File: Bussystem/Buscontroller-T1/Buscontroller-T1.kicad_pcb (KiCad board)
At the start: 2 copper layers, 1 part, among them J1 PCIE-098-02-X-D-TH

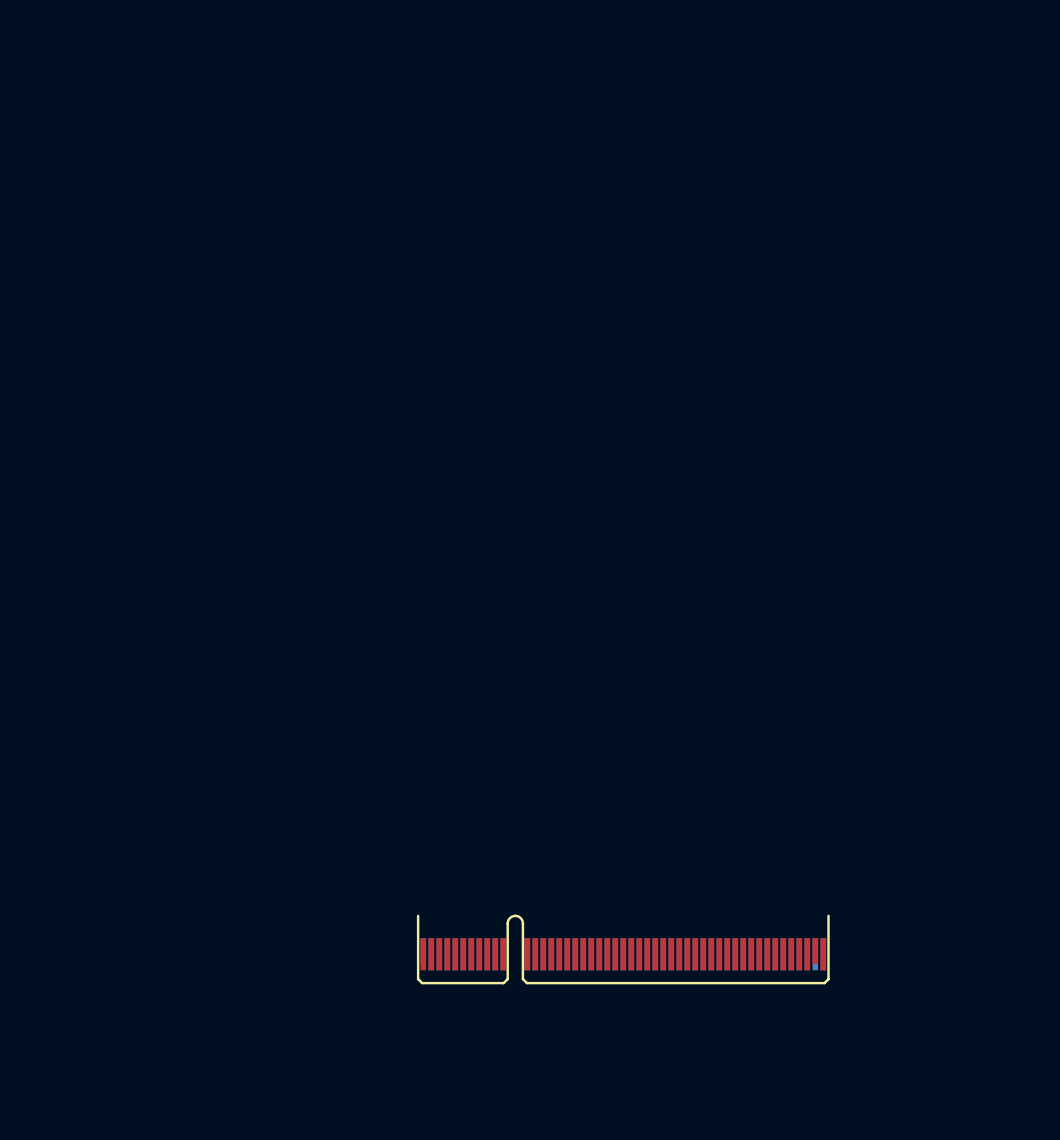
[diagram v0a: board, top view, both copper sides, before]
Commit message: some new parts in the Buscontroller T1
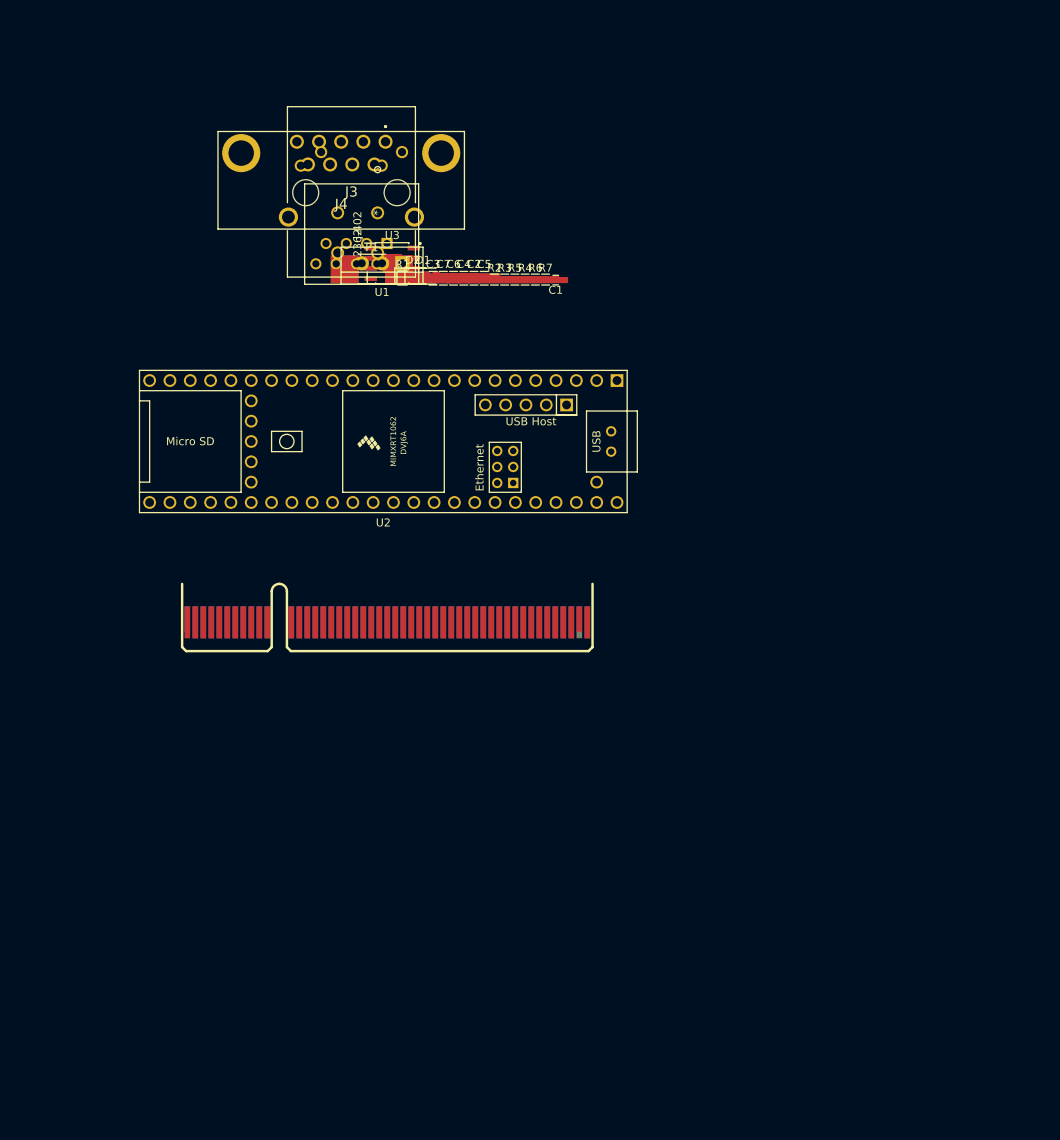
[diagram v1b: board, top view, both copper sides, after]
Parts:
- added C1: 100n, Capacitors_SMD:C_0603_HandSoldering, F.Cu at (125.5, 67.8)
- added C2: 4.7u, Capacitors_SMD:C_0805_HandSoldering, F.Cu at (115.3, 67.6)
- added C3: 100n, Capacitors_SMD:C_0805_HandSoldering, F.Cu at (110.2, 67.6)
- added C4: 100n, Capacitors_SMD:C_0805_HandSoldering, F.Cu at (114.1, 67.6)
- added C5: 100n, Capacitors_SMD:C_0805_HandSoldering, F.Cu at (116.6, 67.6)
- added C6: 100n, Capacitors_SMD:C_0805_HandSoldering, F.Cu at (112.8, 67.6)
- added C7: 4700p, Capacitors_SMD:C_0805_HandSoldering, F.Cu at (111.5, 67.6)
- added D1: 1N4148W, Diodes_SMD:D_SOD-123, F.Cu at (109.0, 67.3)
- added D2: 1N4148W, Diodes_SMD:D_SOD-123, F.Cu at (107.7, 67.3)
- added F1: mSMD050-60V, Resistors_SMD:R_1812_HandSoldering, F.Cu at (102.6, 66.5)
- added J2: 236-402, footprints:236-402, F.Cu at (103.3, 59.4)
- added J3: J1B1211CCD, SamacSys_Parts:J1B1211CCD, F.Cu at (100.0, 56.8)
- added J4: 2311765-1, SamacSys_Parts:23117651, F.Cu at (104.3, 50.5)
- added R1: 0R, Resistors_SMD:R_0805_HandSoldering, F.Cu at (106.4, 67.6)
- added R2: 60R, Resistors_SMD:R_0603_HandSoldering, F.Cu at (117.9, 67.8)
- added R3: 60R, Resistors_SMD:R_0603_HandSoldering, F.Cu at (119.2, 67.8)
- added R4: 1k, Resistors_SMD:R_0603_HandSoldering, F.Cu at (121.7, 67.8)
- added R5: 1k, Resistors_SMD:R_0603_HandSoldering, F.Cu at (120.4, 67.8)
- added R6: 120R, Resistors_SMD:R_0603_HandSoldering, F.Cu at (123.0, 67.8)
- added R7: 120R, Resistors_SMD:R_0603_HandSoldering, F.Cu at (124.3, 67.8)
- added U1: LM7805L-TF3-T, TO_SOT_Packages_THT:TO-220-3_Vertical, F.Cu at (106.4, 65.7)
- added U2: Teensy4.1, teensy:Teensy41, F.Cu at (104.0, 88.0)
- added U3: MCP2542FD, Housings_SOIC:SOIC-8-1EP_3.9x4.9mm_Pitch1.27mm, F.Cu at (105.1, 65.7)
- J1: value PCIE-098-02-X-D-TH -> PCIE-098-edge-conn
- moved J1 50.9 mm to (91.0, 110.0)
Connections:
- J1 pad A1: (no net) -> GND
- J1 pad A10: (no net) -> /CANL
- J1 pad A11: (no net) -> GND
- J1 pad A12: (no net) -> SPI_CS
- J1 pad A13: (no net) -> GND
- J1 pad A14: (no net) -> SPI_Sck
- J1 pad A15: (no net) -> GND
- J1 pad A16: (no net) -> SPI_MoSi
- J1 pad A17: (no net) -> GND
- J1 pad A18: (no net) -> SPI_MiSo
- J1 pad A19: (no net) -> GND
- J1 pad A2: (no net) -> GND
- J1 pad A20: (no net) -> /Do0
- J1 pad A21: (no net) -> /Do1
- J1 pad A22: (no net) -> /Do2
- J1 pad A23: (no net) -> /Do3
- J1 pad A24: (no net) -> /Do4
- J1 pad A25: (no net) -> /Do5
- J1 pad A26: (no net) -> /Do6
- J1 pad A27: (no net) -> /Do7
- J1 pad A28: (no net) -> /Di0
- J1 pad A29: (no net) -> /Di1
- J1 pad A3: (no net) -> /24V
- J1 pad A30: (no net) -> /Di2
- J1 pad A31: (no net) -> /Di3
- J1 pad A32: (no net) -> /Di4
- J1 pad A33: (no net) -> /Di5
- J1 pad A34: (no net) -> /Di6
- J1 pad A35: (no net) -> /Di7
- J1 pad A36: (no net) -> /Dclk
- J1 pad A37: (no net) -> /DWR
- J1 pad A38: (no net) -> Net-(J1-PadA38)
- J1 pad A39: (no net) -> Net-(J1-PadA39)
- J1 pad A4: (no net) -> /24V
- J1 pad A40: (no net) -> Net-(J1-PadA40)
- J1 pad A41: (no net) -> Net-(J1-PadA41)
- J1 pad A42: (no net) -> Net-(J1-PadA42)
- J1 pad A43: (no net) -> Net-(J1-PadA43)
- J1 pad A44: (no net) -> Net-(J1-PadA44)
- J1 pad A45: (no net) -> Net-(J1-PadA45)
- J1 pad A46: (no net) -> Net-(J1-PadA46)
- J1 pad A47: (no net) -> Net-(J1-PadA47)
- J1 pad A48: (no net) -> Net-(J1-PadA48)
- J1 pad A49: (no net) -> Net-(J1-PadA49)
- J1 pad A5: (no net) -> /24V
- J1 pad A6: (no net) -> Scl_I2C
- J1 pad A7: (no net) -> Sda_I2C
- J1 pad A8: (no net) -> /5V
- J1 pad A9: (no net) -> /CANH
- J1 pad B1: (no net) -> GND
- J1 pad B10: (no net) -> /CANL
- J1 pad B11: (no net) -> GND
- J1 pad B12: (no net) -> SPI_CS
- J1 pad B13: (no net) -> GND
- J1 pad B14: (no net) -> SPI_Sck
- J1 pad B15: (no net) -> GND
- J1 pad B16: (no net) -> SPI_MoSi
- J1 pad B17: (no net) -> GND
- J1 pad B18: (no net) -> SPI_MiSo
- J1 pad B19: (no net) -> GND
- J1 pad B2: (no net) -> GND
- J1 pad B20: (no net) -> /Do0
- J1 pad B21: (no net) -> /Do1
- J1 pad B22: (no net) -> /Do2
- J1 pad B23: (no net) -> /Do3
- J1 pad B24: (no net) -> /Do4
- J1 pad B25: (no net) -> /Do5
- J1 pad B26: (no net) -> /Do6
- J1 pad B27: (no net) -> /Do7
- J1 pad B28: (no net) -> /Di0
- J1 pad B29: (no net) -> /Di1
- J1 pad B3: (no net) -> /24V
- J1 pad B30: (no net) -> /Di2
- J1 pad B31: (no net) -> /Di3
- J1 pad B32: (no net) -> /Di4
- J1 pad B33: (no net) -> /Di5
- J1 pad B34: (no net) -> /Di6
- J1 pad B35: (no net) -> /Di7
- J1 pad B36: (no net) -> /Dclk
- J1 pad B37: (no net) -> /DWR
- J1 pad B38: (no net) -> Net-(J1-PadA38)
- J1 pad B39: (no net) -> Net-(J1-PadA39)
- J1 pad B4: (no net) -> /24V
- J1 pad B40: (no net) -> Net-(J1-PadA40)
- J1 pad B41: (no net) -> Net-(J1-PadA41)
- J1 pad B42: (no net) -> Net-(J1-PadA42)
- J1 pad B43: (no net) -> Net-(J1-PadA43)
- J1 pad B44: (no net) -> Net-(J1-PadA44)
- J1 pad B45: (no net) -> Net-(J1-PadA45)
- J1 pad B46: (no net) -> Net-(J1-PadA46)
- J1 pad B47: (no net) -> Net-(J1-PadA47)
- J1 pad B48: (no net) -> Net-(J1-PadA48)
- J1 pad B49: (no net) -> Net-(J1-PadA49)
- J1 pad B5: (no net) -> /24V
- J1 pad B6: (no net) -> Scl_I2C
- J1 pad B7: (no net) -> Sda_I2C
- J1 pad B8: (no net) -> /5V
- J1 pad B9: (no net) -> /CANH

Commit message: erstes import zum Layouten von Buscontroller
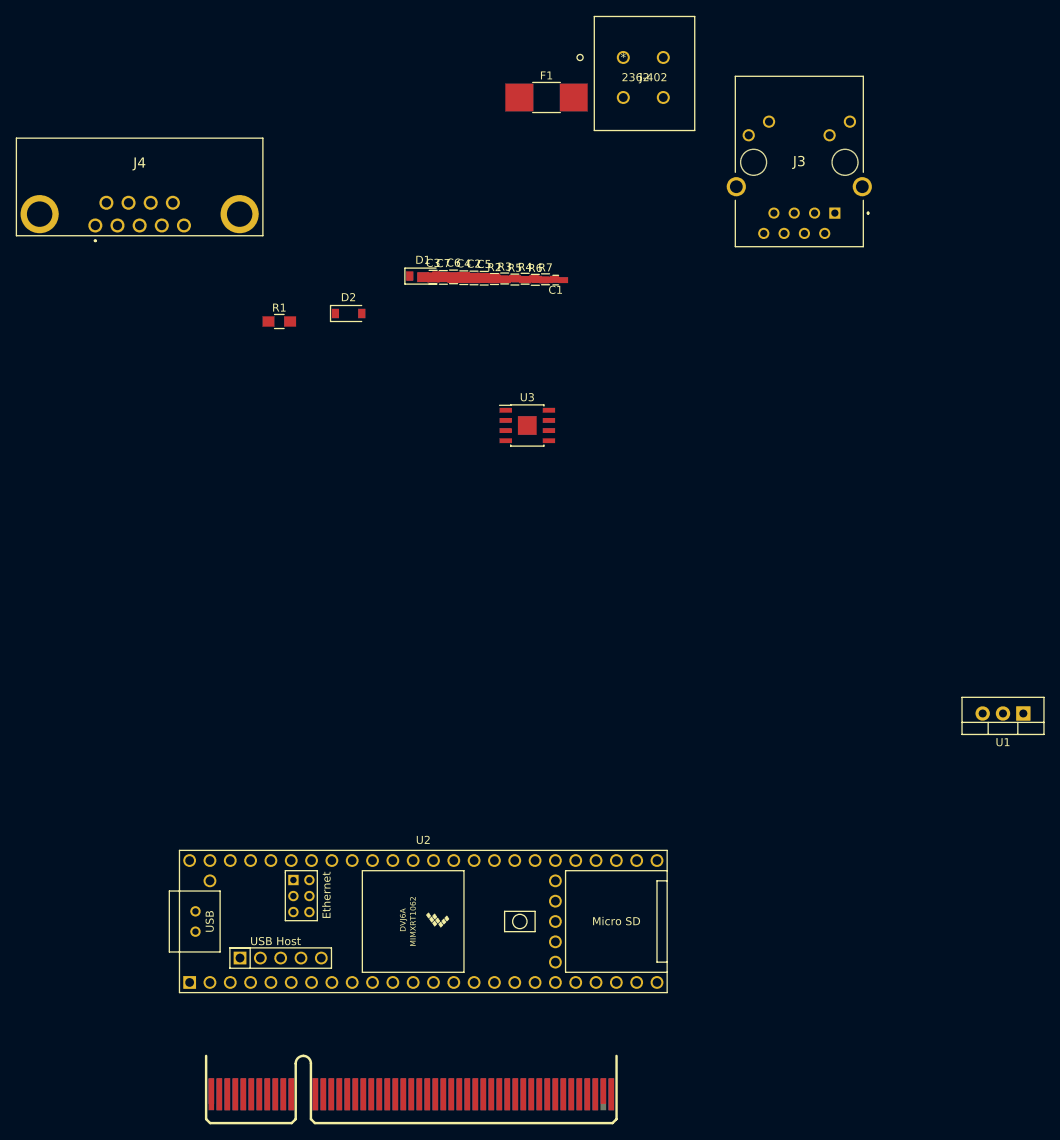
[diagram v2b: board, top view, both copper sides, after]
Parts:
- moved U1 95.9 mm to (184.0, 122.0)
- moved U2 60.2 mm to (109.0, 148.0), turned to 0 degrees
- moved J1 59.1 mm to (94.0, 169.0)
- moved J3 56.1 mm to (156.0, 53.0)
- moved J4 37.8 mm to (68.0, 61.0), turned to 180 degrees
- moved J2 36.3 mm to (134.0, 40.0), turned to 0 degrees
- moved F1 30.6 mm to (124.4, 45.0)
- moved U3 26.4 mm to (122.0, 86.0)
- moved R1 16.3 mm to (91.0, 73.0)
- moved D2 9.29 mm to (99.7, 72.0)
- moved C6 0.17 mm to (112.8, 67.4)
- moved R3 0.14 mm to (119.2, 67.6)
- moved C3 0.13 mm to (110.2, 67.5)
- moved R4 0.10 mm to (121.7, 67.7)
- moved C7 0.10 mm to (111.5, 67.5)
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
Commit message: buscontroller T1 fertig
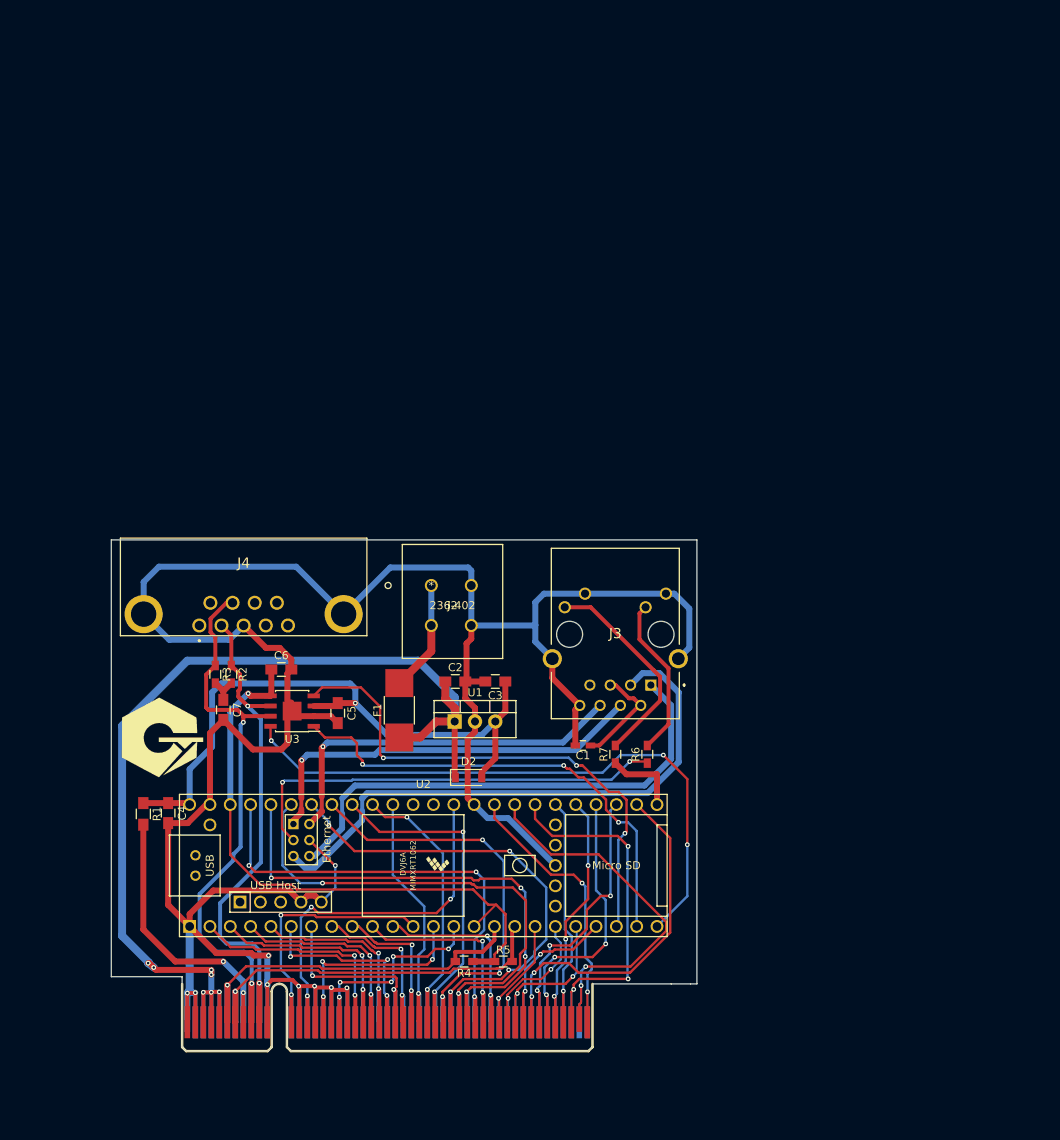
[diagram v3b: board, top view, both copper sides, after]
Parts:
- removed D1: 1N4148W, Diodes_SMD:D_SOD-123
- added G***: Gyurmas Electronix, Gyurmas:GyLogo2_1, F.Cu at (76.4, 125.0)
- J3: footprint SamacSys_Parts:J1B1211CCD -> J1B1211CCD
- J4: footprint SamacSys_Parts:23117651 -> 23117651
- moved R4 85.7 mm to (114.1, 153.0), turned to 180 degrees
- moved R5 85.3 mm to (119.0, 153.0)
- moved F1 78.8 mm to (106.0, 121.6), turned to 90 degrees
- moved C4 76.5 mm to (77.1, 134.4), turned to 270 degrees
- moved U1 71.1 mm to (112.9, 123.0), turned to 0 degrees
- moved J2 70.2 mm to (110.0, 106.0)
- moved R1 63.9 mm to (74.0, 134.6), turned to 270 degrees
- moved J3 63.3 mm to (133.0, 112.0)
- moved R3 61.3 mm to (83.0, 117.1), turned to 270 degrees
- moved R6 60.9 mm to (137.0, 127.1), turned to 90 degrees
- moved C7 60.7 mm to (84.0, 121.5), turned to 270 degrees
- moved R7 60.0 mm to (133.0, 127.1), turned to 90 degrees
- moved D2 59.9 mm to (114.7, 130.0)
- moved R2 59.4 mm to (85.0, 117.1), turned to 270 degrees
- moved C1 58.3 mm to (128.9, 126.0)
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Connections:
- net Net-(U2-Pad22) renamed /CANRX3
- net Net-(U2-Pad23) renamed /CANTX3
- net Net-(U2-Pad24) renamed /CANStby
- C4 pad 1: Net-(C4-Pad1) -> Net-(C3-Pad1)
- C5 pad 1: Net-(C4-Pad1) -> Net-(C3-Pad1)
- J1 pad A38: Net-(J1-PadA38) -> /D0
- J1 pad A39: Net-(J1-PadA39) -> /D1
- J1 pad A40: Net-(J1-PadA40) -> /D2
- J1 pad A41: Net-(J1-PadA41) -> /D3
- J1 pad A42: Net-(J1-PadA42) -> /D4
- J1 pad A43: Net-(J1-PadA43) -> /D5
- J1 pad A44: Net-(J1-PadA44) -> /D6
- J1 pad A45: Net-(J1-PadA45) -> /D7
- J1 pad A46: Net-(J1-PadA46) -> /D8
- J1 pad A47: Net-(J1-PadA47) -> /D9
- J1 pad A48: Net-(J1-PadA48) -> /D10
- J1 pad A49: Net-(J1-PadA49) -> /D11
- J1 pad B38: Net-(J1-PadA38) -> /D0
- J1 pad B39: Net-(J1-PadA39) -> /D1
- J1 pad B40: Net-(J1-PadA40) -> /D2
- J1 pad B41: Net-(J1-PadA41) -> /D3
- J1 pad B42: Net-(J1-PadA42) -> /D4
- J1 pad B43: Net-(J1-PadA43) -> /D5
- J1 pad B44: Net-(J1-PadA44) -> /D6
- J1 pad B45: Net-(J1-PadA45) -> /D7
- J1 pad B46: Net-(J1-PadA46) -> /D8
- J1 pad B47: Net-(J1-PadA47) -> /D9
- J1 pad B48: Net-(J1-PadA48) -> /D10
- J1 pad B49: Net-(J1-PadA49) -> /D11
- R1 pad 1: Net-(C4-Pad1) -> Net-(C3-Pad1)
- U2 pad 15: (no net) -> +3V3
- U2 pad 18: (no net) -> /D0
- U2 pad 19: (no net) -> /D1
- U2 pad 20: (no net) -> /D2
- U2 pad 21: (no net) -> /D3
- U2 pad 26: (no net) -> /D4
- U2 pad 27: (no net) -> /D5
- U2 pad 28: (no net) -> /D6
- U2 pad 29: (no net) -> /D7
- U2 pad 30: (no net) -> /D8
- U2 pad 31: (no net) -> /D9
- U2 pad 32: (no net) -> /D10
- U2 pad 33: (no net) -> /D11
- U2 pad 48: Net-(C4-Pad1) -> Net-(C3-Pad1)
- U3 pad 3: Net-(C4-Pad1) -> Net-(C3-Pad1)
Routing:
- net GND: track 0.00 -> 364.6 mm, vias 0 -> 9
- net /24V: track 0.00 -> 140.6 mm, vias 0 -> 7
- net Net-(C3-Pad1): track 0.00 -> 79.9 mm, vias 0 -> 1
- net +3V3: track 0.00 -> 77.9 mm, vias 0 -> 1
- net /CANStby: track 0.00 -> 77.6 mm, vias 0 -> 3
- net /CANH: track 0.00 -> 74.2 mm, vias 0 -> 2
- net /T-: track 0.00 -> 72.3 mm
- net /Di6: track 0.00 -> 67.5 mm, vias 0 -> 4
- net /CANL: track 0.00 -> 65.6 mm, vias 0 -> 2
- net /Di5: track 0.00 -> 65.4 mm, vias 0 -> 2
- net /CANRX3: track 0.00 -> 65.2 mm, vias 0 -> 3
- net /Di4: track 0.00 -> 63.1 mm, vias 0 -> 4
- net /T+: track 0.00 -> 62.7 mm
- net /CANTX3: track 0.00 -> 59.6 mm, vias 0 -> 3
- net /Di7: track 0.00 -> 59.4 mm, vias 0 -> 3
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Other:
- board outline added: 73.2 x 63.9 mm
